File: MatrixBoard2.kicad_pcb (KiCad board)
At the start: 2 copper layers, 70 x 60 mm, 197 parts, among them J1 Conn_01x03_Male, J2 Conn_01x03_Male

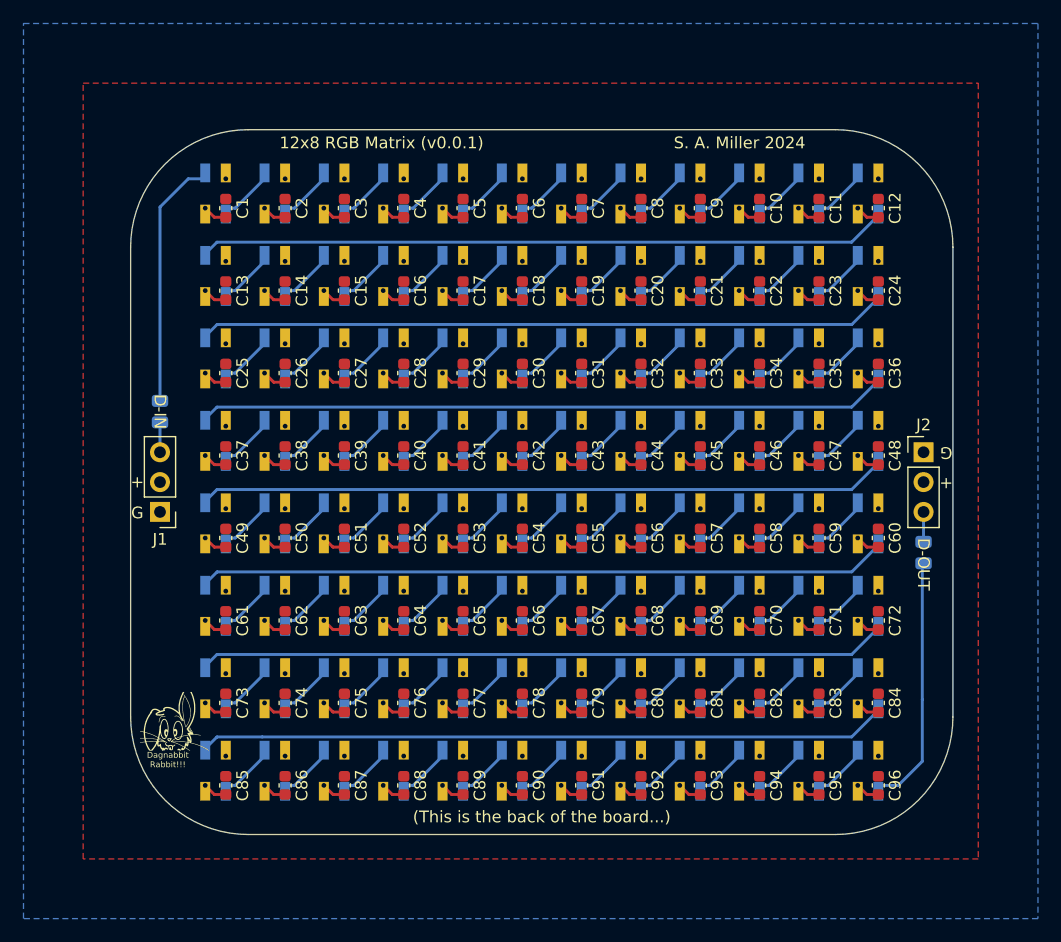
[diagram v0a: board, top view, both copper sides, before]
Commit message: Added possible Bulk Capacitance...
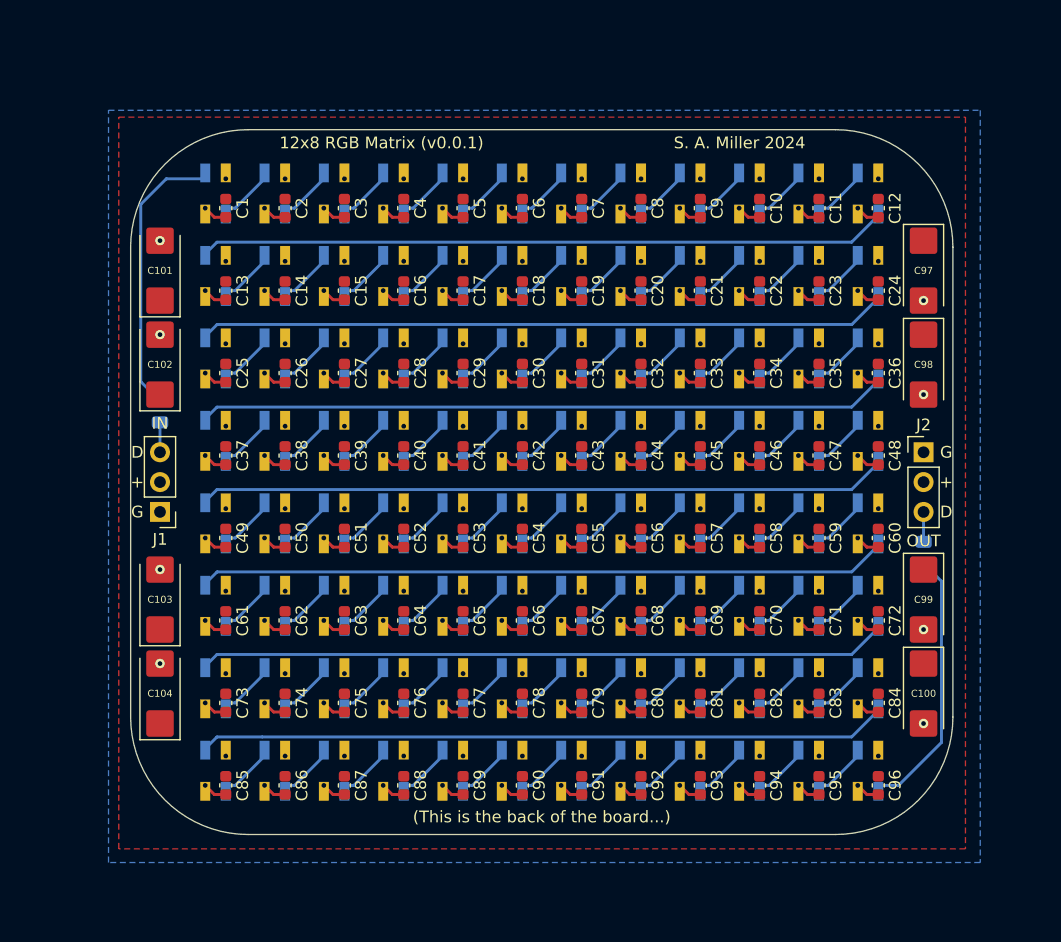
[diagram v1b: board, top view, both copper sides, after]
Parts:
- removed REF**: DagNabbit, Rabbit:DagNabbit
- added C100: 100uf, Capacitor_Tantalum_SMD:CP_EIA-6032-28_Kemet-C_Pad2.25x2.35mm_HandSolder, F.Cu at (132.5, 118.0)
- added C101: 100uf, Capacitor_Tantalum_SMD:CP_EIA-6032-28_Kemet-C_Pad2.25x2.35mm_HandSolder, F.Cu at (67.5, 82.0)
- added C102: 100uf, Capacitor_Tantalum_SMD:CP_EIA-6032-28_Kemet-C_Pad2.25x2.35mm_HandSolder, F.Cu at (67.5, 90.0)
- added C103: 100uf, Capacitor_Tantalum_SMD:CP_EIA-6032-28_Kemet-C_Pad2.25x2.35mm_HandSolder, F.Cu at (67.5, 110.0)
- added C104: 100uf, Capacitor_Tantalum_SMD:CP_EIA-6032-28_Kemet-C_Pad2.25x2.35mm_HandSolder, F.Cu at (67.5, 118.0)
- added C97: 100uf, Capacitor_Tantalum_SMD:CP_EIA-6032-28_Kemet-C_Pad2.25x2.35mm_HandSolder, F.Cu at (132.5, 82.0)
- added C98: 100uf, Capacitor_Tantalum_SMD:CP_EIA-6032-28_Kemet-C_Pad2.25x2.35mm_HandSolder, F.Cu at (132.5, 90.0)
- added C99: 100uf, Capacitor_Tantalum_SMD:CP_EIA-6032-28_Kemet-C_Pad2.25x2.35mm_HandSolder, F.Cu at (132.5, 110.0)
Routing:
- net Net-(D1-Pad3): track 21.3 -> 23.8 mm
- net Net-(D96-Pad1): track 21.5 -> 22.8 mm
- net GND: vias 0 -> 8
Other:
- board text added: "D"
- board text added: "IN"
- board text added: "OUT"
- board text removed: "D-IN"
- board text removed: "D-OUT"
